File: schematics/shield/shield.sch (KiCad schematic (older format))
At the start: 44 parts, among them P1 CONN_01X05, P2 CONN_01X03, P3 CONN_01X02, P4 CONN_01X03, P5 CONN_01X03, SW1 SW_PUSH, SW2 SW_PUSH, U1 ArduinoProMicro, U2 INA2126, U3 MCP3301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

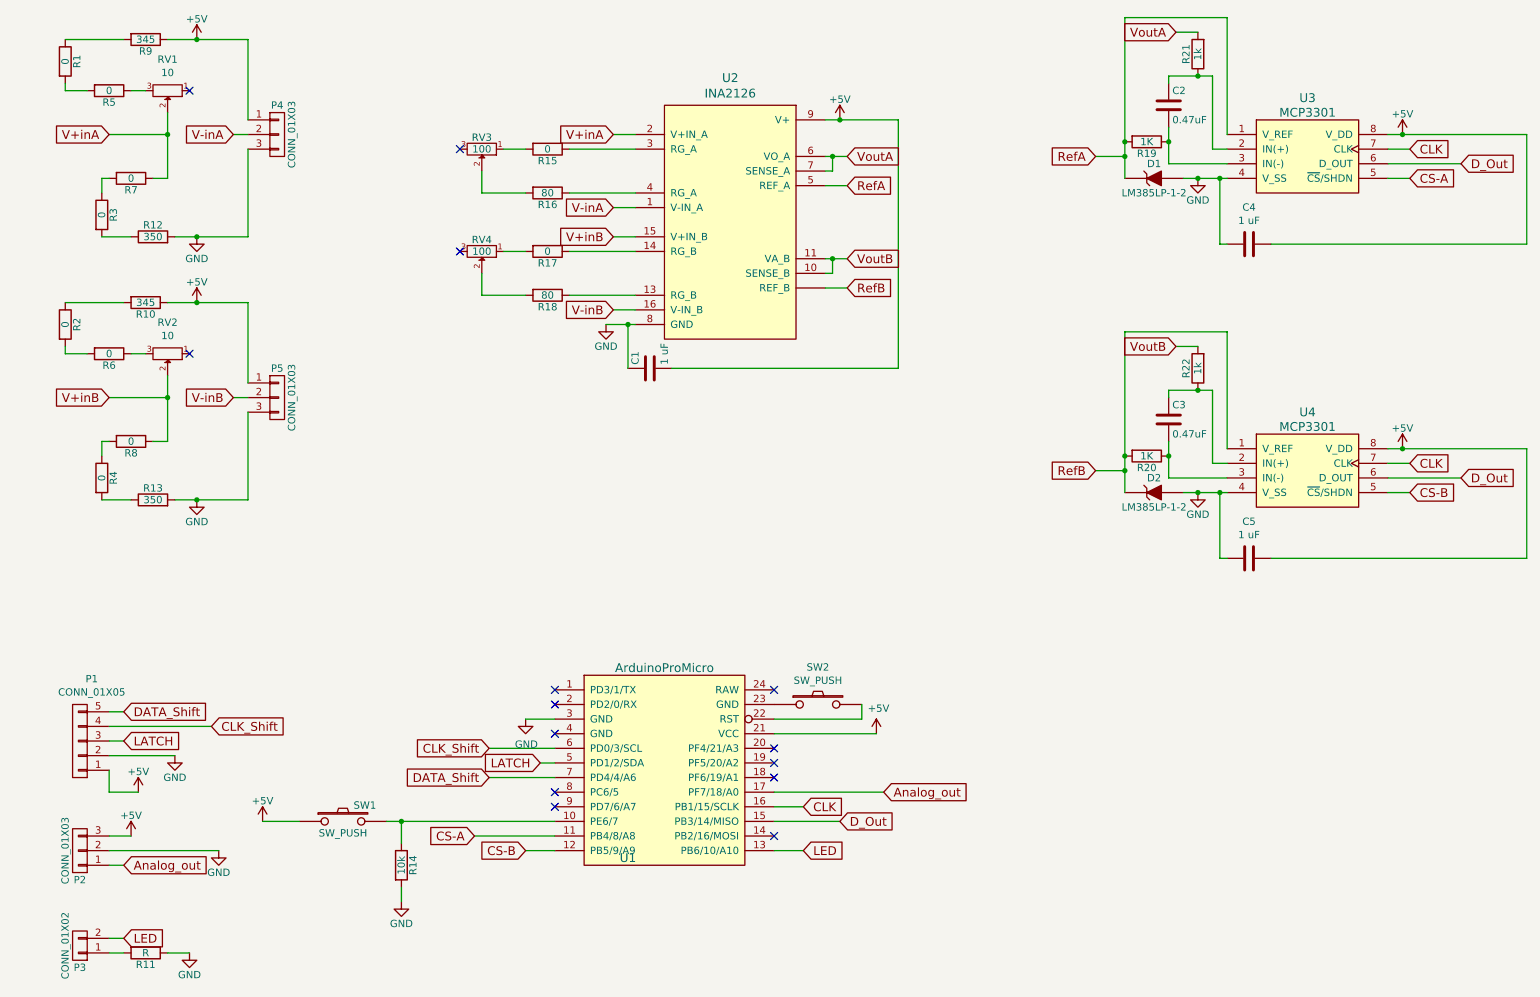
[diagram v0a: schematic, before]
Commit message: Change symbol for the strain gauges
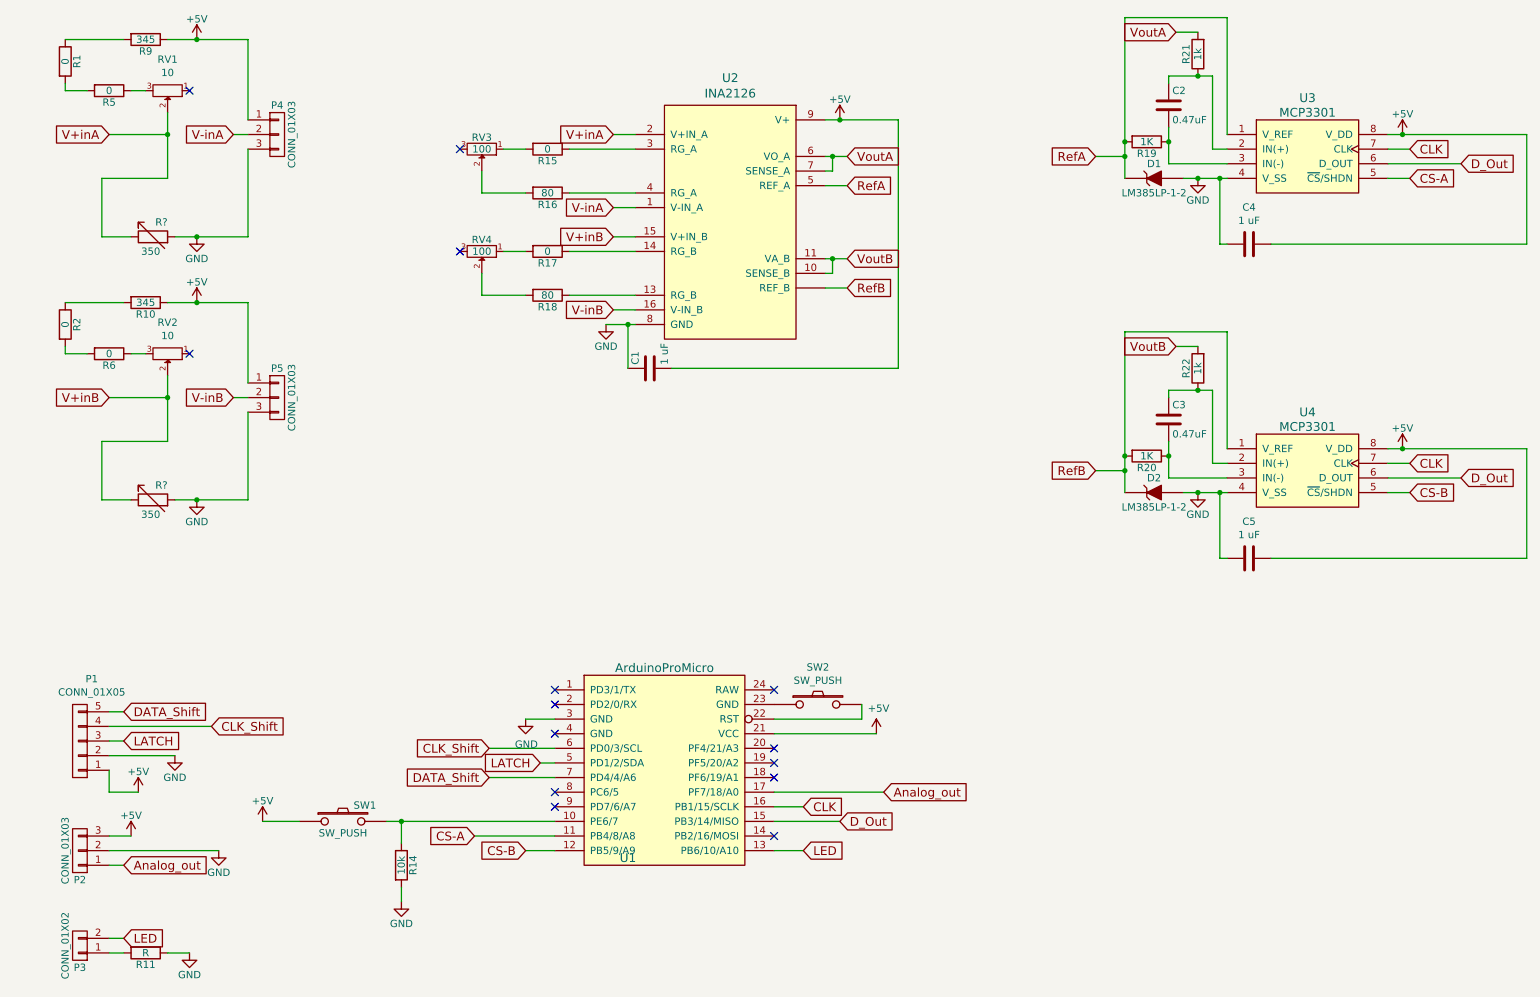
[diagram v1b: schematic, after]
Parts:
- removed R12, R13: 350, Resistors_SMD:R_0603, symbol R
- removed R3, R4, R7, R8: 0, Resistors_SMD:R_0603, symbol R
- added R? (x2): 350, symbol R_Variable
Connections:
- net GND: now also R?.2, R?.2
- net V+inA: now also R?.1
- net V+inB: now also R?.1

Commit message: Change configuration of the trim-pots for the bridge
This change effects a easier calibration as it is less sensitive to
changes.
Furthermore it also seems to eliminate a certain creeping of the signal
that was present before.
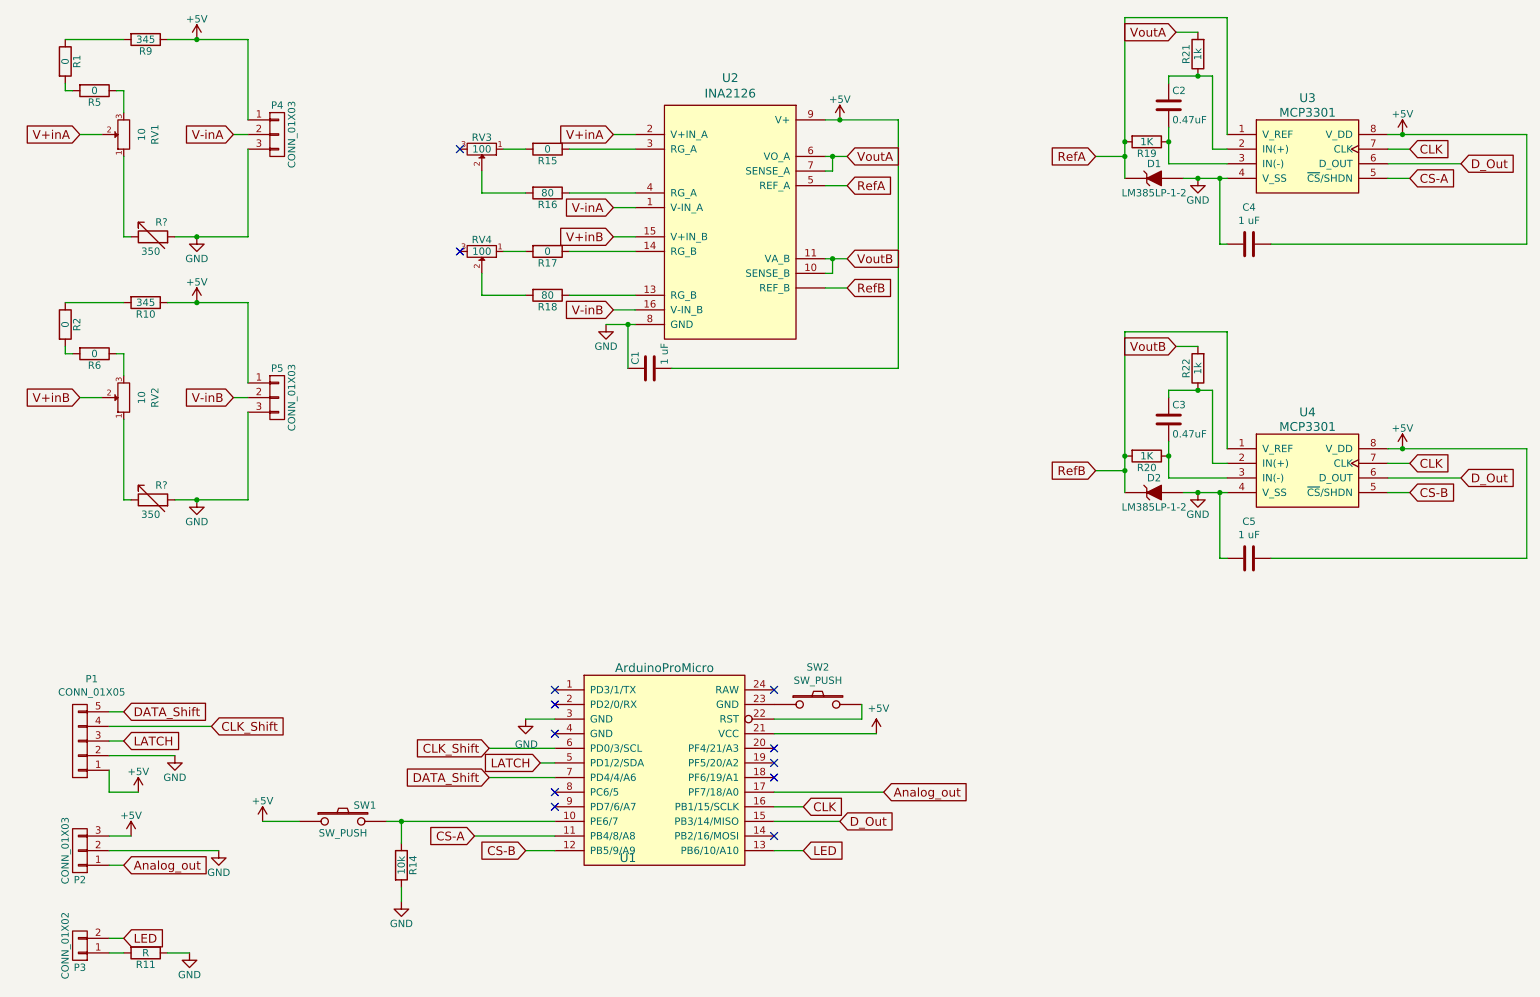
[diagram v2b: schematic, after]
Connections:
- net V+inA: no longer R?.1
- net V+inB: no longer R?.1
- net at RV1.1: now also R?.1
- net at RV2.1: now also R?.1
- no-connect marks 14 -> 12
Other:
- moved on the sheet: R5, R6, RV1, RV2
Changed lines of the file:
@@
 Text GLabel 4600 2100 0    60   Input ~ 0
 V+inB
-Text GLabel 1150 1400 0    60   Input ~ 0
+Text GLabel 950  1400 0    60   Input ~ 0
 V+inA
 $Comp
@@
 L POT-RESCUE-shield RV1
 U 1 1 57D5BE3A
-P 1550 1100
-F 0 "RV1" H 1550 886 50  0000 C CNN
-F 1 "10" H 1550 977 50  0000 C CNN
-F 2 "Potentiometers:Potentiometer_Bourns_3296Y_3-8Zoll_Angular_ScrewUp" H 1550 1100 50  0001 C CNN
-F 3 "" H 1550 1100 50  0000 C CNN
-	1    1550 1100
-	-1   0    0    1
+P 1250 1400
+F 0 "RV1" H 1250 1186 50  0000 C CNN
+F 1 "10" H 1250 1277 50  0000 C CNN
+F 2 "Potentiometers:Potentiometer_Bourns_3296Y_3-8Zoll_Angular_ScrewUp" H 1250 1400 50  0001 C CNN
+F 3 "" H 1250 1400 50  0000 C CNN
+	1    1250 1400
+	0    -1   -1   0
 $EndComp
 $Comp
@@
 L R R5
 U 1 1 581DD452
-P 1150 1100
-F 0 "R5" V 1230 1100 50  0000 C CNN
-F 1 "0" V 1150 1100 50  0000 C CNN
-F 2 "Resistors_SMD:R_0603" V 1080 1100 50  0001 C CNN
-F 3 "" H 1150 1100 50  0000 C CNN
-	1    1150 1100
+P 1050 1100
+F 0 "R5" V 1130 1100 50  0000 C CNN
+F 1 "0" V 1050 1100 50  0000 C CNN
+F 2 "Resistors_SMD:R_0603" V 980 1100 50  0001 C CNN
+F 3 "" H 1050 1100 50  0000 C CNN
+	1    1050 1100
 	0    1    1    0
 $EndComp
@@
 	0    1    1    0
 $EndComp
-Text GLabel 1150 3200 0    60   Input ~ 0
+Text GLabel 950  3200 0    60   Input ~ 0
 V+inB
 $Comp
@@
 L POT-RESCUE-shield RV2
 U 1 1 581DE3CB
-P 1550 2900
-F 0 "RV2" H 1550 2686 50  0000 C CNN
-F 1 "10" H 1550 2777 50  0000 C CNN
-F 2 "Potentiometers:Potentiometer_Bourns_3296Y_3-8Zoll_Angular_ScrewUp" H 1550 2900 50  0001 C CNN
-F 3 "" H 1550 2900 50  0000 C CNN
-	1    1550 2900
-	-1   0    0    1
+P 1250 3200
+F 0 "RV2" H 1250 2986 50  0000 C CNN
+F 1 "10" H 1250 3077 50  0000 C CNN
+F 2 "Potentiometers:Potentiometer_Bourns_3296Y_3-8Zoll_Angular_ScrewUp" H 1250 3200 50  0001 C CNN
+F 3 "" H 1250 3200 50  0000 C CNN
+	1    1250 3200
+	0    -1   -1   0
 $EndComp
 Text GLabel 2000 3200 0    60   Input ~ 0
@@
 L R R6
 U 1 1 581DE3E0
-P 1150 2900
-F 0 "R6" V 1230 2900 50  0000 C CNN
-F 1 "0" V 1150 2900 50  0000 C CNN
-F 2 "Resistors_SMD:R_0603" V 1080 2900 50  0001 C CNN
-F 3 "" H 1150 2900 50  0000 C CNN
-	1    1150 2900
+P 1050 2900
+F 0 "R6" V 1130 2900 50  0000 C CNN
+F 1 "0" V 1050 2900 50  0000 C CNN
+F 2 "Resistors_SMD:R_0603" V 980 2900 50  0001 C CNN
+F 3 "" H 1050 2900 50  0000 C CNN
+	1    1050 2900
 	0    1    1    0
 $EndComp
@@
 	1    0    0    -1
 $EndComp
-NoConn ~ 1700 2900
-NoConn ~ 1700 1100
 $Comp
 L R R15
@@
 	8800 1500 8700 1500
 Wire Wire Line
-	8700 1500 8700 1000
-Wire Wire Line
-	8700 1000 8400 1000
+	8700 1000 8700 1500
+Wire Wire Line
+	8400 1000 8700 1000
 Wire Wire Line
 	8400 1000 8400 1050
@@
 	8800 3650 8700 3650
 Wire Wire Line
-	8700 3650 8700 3150
-Wire Wire Line
-	8700 3150 8400 3150
+	8700 3150 8700 3650
+Wire Wire Line
+	8400 3150 8700 3150
 Wire Wire Line
 	8400 3150 8400 3200
@@
 	850  1050 850  1100
 Wire Wire Line
-	850  1100 1000 1100
-Wire Wire Line
-	1300 1100 1400 1100
+	850  1100 900  1100
+Wire Wire Line
+	1200 1100 1250 1100
 Wire Wire Line
 	1250 750  850  750
 Wire Wire Line
-	1100 2100 1300 2100
+	1250 2100 1300 2100
 Wire Wire Line
 	1600 2100 2100 2100
-Wire Wire Line
-	1150 3200 1550 3200
-Connection ~ 1550 3200
 Connection ~ 1750 3900
 Wire Wire Line
@@
 	850  2850 850  2900
 Wire Wire Line
-	850  2900 1000 2900
-Wire Wire Line
-	1300 2900 1400 2900
+	850  2900 900  2900
+Wire Wire Line
+	1200 2900 1250 2900
 Wire Wire Line
 	1250 2550 850  2550
 Wire Wire Line
-	1100 3900 1300 3900
-Wire Wire Line
 	1600 3900 2100 3900
-Wire Wire Line
-	1100 3500 1550 3500
-Wire Wire Line
-	1550 3500 1550 3050
 Wire Wire Line
 	3850 1500 4000 1500
@@
 	1150 5900 1350 5900
 Wire Wire Line
-	1100 1700 1550 1700
-Connection ~ 1550 1400
-Wire Wire Line
-	1550 1700 1550 1250
-Wire Wire Line
-	1150 1400 1550 1400
-Wire Wire Line
-	1100 1700 1100 2100
-Wire Wire Line
-	1100 3500 1100 3900
+	1250 1100 1250 1250
+Wire Wire Line
+	950  1400 1100 1400
+Wire Wire Line
+	1250 3350 1250 3900
+Wire Wire Line
+	1100 3200 950  3200
+Wire Wire Line
+	1250 2900 1250 3050
+Wire Wire Line
+	1250 3900 1300 3900
+Wire Wire Line
+	1250 2100 1250 1550
 $EndSCHEMATC
